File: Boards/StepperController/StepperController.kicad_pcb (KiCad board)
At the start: 2 copper layers, 160 x 100 mm, 131 parts, among them IC1 ATMEGA645A-A, J1 I2C, J2 SPI_Extern, J3 ISP, J4 Reference, J5 Display, J7 Spindle, P1 Power, P10 CONN_Z, P3 USB_B, P4 Relay2, P5 Relay1, P7 EmerOff, P8 CONN_X, P9 CONN_Y, Q1 BC817-40, Q2 BC817-40, Q3 BC817-40, Q4 BC817-40, Q5 BC817-40, SW2 SW_1, SW3 SW_2, U1 LM2595S-5, U3 FT232RL, U4 74LS08, U5 TMC2660, U6 TMC2660, U7 TMC2660, U8 74HC00, X1 16MHz

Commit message: Work in Progress
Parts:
- removed C14: 100nF, Capacitors_SMD:C_0805_HandSoldering
- removed RR1: 10k, w_pth_resistors:r-sil_8
- removed U4: 74LS08, Housings_SOIC:SOIC-14_3.9x8.7mm_Pitch1.27mm
- added D13, D14, D15, D16, D17, D18, D19, D21, D22, D23: 5V, w_smd_diode:sod123, F.Cu at (37.1, 68.1)
- added D20: 6V, w_smd_diode:sod123, F.Cu at (37.1, 68.1)
- added R42: 10k, Resistors_SMD:R_0805_HandSoldering, B.Cu at (197.6, 65.5)
- added R43: 10k, Resistors_SMD:R_0805_HandSoldering, B.Cu at (200.7, 65.5)
- added R44: 10k, Resistors_SMD:R_0805_HandSoldering, B.Cu at (203.7, 65.5)
- added R45: 10k, Resistors_SMD:R_0805_HandSoldering, B.Cu at (206.8, 65.5)
- added R46: 10k, Resistors_SMD:R_0805_HandSoldering, B.Cu at (209.8, 65.5)
- added R47: 10k, Resistors_SMD:R_0805_HandSoldering, B.Cu at (212.9, 65.5)
- added R48: 10k, Resistors_SMD:R_0805_HandSoldering, B.Cu at (215.9, 65.5)
- added R49: 10k, Resistors_SMD:R_0805_HandSoldering, F.Cu at (33.5, 104.1)
- added R50: 10k, Resistors_SMD:R_0805_HandSoldering, F.Cu at (40.1, 104.1)
- added R51: 10k, Resistors_SMD:R_0805_HandSoldering, F.Cu at (33.5, 97.5)
- added R52: 10k, Resistors_SMD:R_0805_HandSoldering, F.Cu at (40.1, 97.5)
- added R53: 100k, Resistors_SMD:R_0805_HandSoldering, F.Cu at (42.2, 110.2)
- added R54: 100k, Resistors_SMD:R_0805_HandSoldering, F.Cu at (26.9, 112.3)
- added R55: 10k, Resistors_SMD:R_0805_HandSoldering, F.Cu at (37.1, 68.1)
- added R56: 4k7, Resistors_SMD:R_0805_HandSoldering, F.Cu at (26.9, 119.4)
- added R57: 4k7, Resistors_SMD:R_0805_HandSoldering, F.Cu at (34.0, 119.4)
- R2, R36, R37, R38, R39, R40, R41: moved to B.Cu
- SW2, SW3: footprint w_switch:smd_push -> SW0773:SW_0773
- X1: footprint Oscillator-Modules:OSCILLATOR_KXO-200_LargePads -> Oscillators:KXO-200_LargePads
- moved R41 231.1 mm to (217.4, 78.2), turned to 90 degrees
- moved R40 228.2 mm to (214.4, 78.2), turned to 90 degrees
- moved R39 225.3 mm to (211.3, 78.2), turned to 90 degrees
- moved R38 222.5 mm to (208.3, 78.2), turned to 90 degrees
- moved R37 219.6 mm to (205.2, 78.2), turned to 90 degrees
- moved R36 216.8 mm to (202.2, 78.2), turned to 90 degrees
- moved R2 214.0 mm to (199.1, 78.2), turned to 90 degrees
- moved C46 71.0 mm to (218.4, 86.9), turned to 270 degrees
- moved U8 70.2 mm to (210.8, 89.4)
- moved C1 27.5 mm to (212.3, 134.1)
- moved J4 12.7 mm to (208.8, 71.1)
- moved SW3 11.6 mm to (174.8, 151.4)
- moved J1 11.2 mm to (186.9, 146.3)
- moved SW2 5.08 mm to (161.5, 151.4)
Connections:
- C2 pad 1: +5V -> Net-(C2-Pad1)
- C7 pad 1: +5V -> Net-(C7-Pad1)
- IC1 pad 34: (no net) -> /Interface/Ref_T1
- IC1 pad 35: /Controller/Ref_X1 -> /Controller/Ref_Z1
- IC1 pad 37: /Controller/Ref_Z1 -> /Controller/Ref_X1
- IC1 pad 41: /Interface/Ref_T1 -> (no net)
- IC1 pad 62: +5V -> Net-(C7-Pad1)
- J5 pad 2: /Controller/SCK -> Net-(J5-Pad2)
- J5 pad 3: /Controller/SDI -> Net-(J5-Pad3)
- J5 pad 4: /Controller/SDO -> Net-(J5-Pad4)
- J5 pad 5: /Interface/CS_Disp -> Net-(J5-Pad5)
- J7 pad 2: /Controller/Spindle_PWM -> Net-(D22-Pad1)
- J7 pad 3: /Interface/Spindle_Enable -> Net-(D23-Pad1)
- L1 pad 2: +5V -> Net-(C2-Pad1)
- P1 pad 1: /Driver/Sup_36V -> (no net)
- R1 pad 1: +5V -> Net-(C2-Pad1)
- U1 pad 4: +5V -> Net-(C2-Pad1)
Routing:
- net /Controller/Ref_X1: track 0.00 -> 142.5 mm, vias 0 -> 3
- net /Controller/Spindle_PWM: track 96.5 -> 0.00 mm, vias 1 -> 0
- net Net-(IC1-Pad40): track 27.5 -> 103.0 mm, vias 0 -> 2
- net /Controller/Stall_Z: track 54.1 -> 127.8 mm, vias 2 -> 4
- net Net-(IC1-Pad39): track 30.4 -> 100.9 mm, vias 0 -> 2
- net /Interface/Spindle_Enable: track 69.4 -> 0.00 mm, vias 1 -> 0
- net Net-(IC1-Pad38): track 35.9 -> 101.9 mm, vias 0 -> 2
- net /Controller/Stall_Y: track 26.3 -> 91.6 mm, vias 2 -> 4
- net +5V: track 257.6 -> 202.7 mm, vias 10 -> 8
- net /Controller/SDI: track 248.4 -> 219.6 mm, vias 7 -> 6
- net Net-(C2-Pad1): track 0.00 -> 17.4 mm
- net /Controller/Ref_Y2: track 0.00 -> 15.6 mm, vias 0 -> 1
- net /Controller/Ref_Z2: track 0.00 -> 14.7 mm, vias 0 -> 1
- net /Controller/Ref_X2: track 0.00 -> 13.2 mm, vias 0 -> 1
- net Net-(D13-Pad1): track 0.01 -> 12.8 mm
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
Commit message: Recover from damaged repository
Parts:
- removed REF**: EuroBoard160mmX100mm_holes, Euro:EuroBoard160mmX100mm_holes
- added D24: D, Diodes_SMD:SOD-123, F.Cu at (90.4, 113.8)
- added D25: D, Diodes_SMD:SOD-123, F.Cu at (86.4, 113.8)
- added F2: 4AT, Fuse_Holders_and_Fuses:Fuseholder5x20_horiz_open_universal_Type-III, F.Cu at (198.6, 160.0)
- C10, C11, C12, C7: moved to F.Cu
- D13, D14, D15, D16, D17, D18, D19, D20: footprint w_smd_diode:sod123 -> Diodes_SMD:SOD-123
- D21, D22, D23: footprint w_smd_diode:sod123 -> Diodes_SMD:SOD-123; moved to B.Cu
- R49, R50, R51, R52: moved to B.Cu
- moved D19 180.1 mm to (216.9, 77.2), turned to 270 degrees
- moved D18 177.5 mm to (214.4, 77.2), turned to 270 degrees
- moved D17 175.0 mm to (211.8, 77.2), turned to 270 degrees
- moved D16 172.5 mm to (209.3, 77.2), turned to 270 degrees
- moved D15 169.9 mm to (206.8, 77.2), turned to 270 degrees
- moved D20 169.2 mm to (193.0, 133.6)
- moved D14 167.4 mm to (204.2, 77.2), turned to 270 degrees
- moved D13 164.8 mm to (201.7, 77.2), turned to 270 degrees
- moved R51 98.6 mm to (122.9, 139.2), turned to 90 degrees
- moved R52 95.0 mm to (125.5, 139.2), turned to 90 degrees
- moved R49 93.7 mm to (120.4, 139.2), turned to 90 degrees
- moved R50 85.3 mm to (117.9, 139.2), turned to 90 degrees
- moved R56 82.9 mm to (105.2, 146.8), turned to 90 degrees
- moved J1 80.9 mm to (106.2, 140.7)
- moved R57 78.6 mm to (107.7, 146.8), turned to 90 degrees
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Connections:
- D1 pad 2: (no net) -> GND
- IC1 pad 10: (no net) -> /Interface/CS_Disp
- IC1 pad 14: Net-(IC1-Pad14) -> (no net)
- IC1 pad 15: Net-(IC1-Pad15) -> (no net)
- IC1 pad 16: Net-(IC1-Pad16) -> (no net)
- IC1 pad 26: /Controller/Emergency_Off -> (no net)
- IC1 pad 27: /Interface/Spindle_Enable -> Net-(IC1-Pad27)
- IC1 pad 28: /Controller/Enable -> Net-(IC1-Pad28)
- IC1 pad 29: (no net) -> Net-(IC1-Pad29)
- IC1 pad 43: /Interface/CS_Disp -> (no net)
- IC1 pad 54: (no net) -> /Interface/Spindle_Enable
- IC1 pad 55: (no net) -> /Controller/Enable
- IC1 pad 56: (no net) -> /Controller/Emergency_Off
- J2 pad 5: Net-(IC1-Pad14) -> Net-(IC1-Pad27)
- J2 pad 6: Net-(IC1-Pad15) -> Net-(IC1-Pad28)
- J2 pad 7: Net-(IC1-Pad16) -> Net-(IC1-Pad29)
- P1 pad 1: (no net) -> /Driver/Sup_36V
- R1 pad 1: Net-(C2-Pad1) -> +5V
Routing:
- net /Interface/Ref_T1: track 1.06 -> 119.4 mm, vias 0 -> 3
- net /Controller/Ref_Y1: track 2.65 -> 119.0 mm, vias 0 -> 3
- net /Controller/Ref_Z1: track 1.52 -> 116.6 mm, vias 0 -> 3
- net /Controller/Spindle_PWM: track 0.00 -> 64.4 mm, vias 0 -> 2
- net Net-(IC1-Pad9): track 0.00 -> 62.7 mm
- net Net-(IC1-Pad29): track 0.00 -> 52.6 mm, vias 0 -> 1
- net Net-(IC1-Pad28): track 0.00 -> 50.3 mm, vias 0 -> 1
- net Net-(IC1-Pad27): track 0.00 -> 48.9 mm, vias 0 -> 1
- net Net-(IC1-Pad8): track 0.00 -> 48.7 mm
- net /Controller/SCK: track 209.0 -> 255.1 mm, vias 6 -> 8
- net /Interface/Spindle_Enable: track 0.00 -> 45.6 mm
- net +5V: track 202.7 -> 245.0 mm, vias 8 -> 6
- net /Controller/SDI: track 219.6 -> 259.8 mm
- net /Controller/SDO: track 202.2 -> 240.2 mm, vias 4 -> 6
- net Net-(D4-Pad2): track 0.00 -> 29.9 mm, vias 0 -> 1
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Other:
- board outline removed

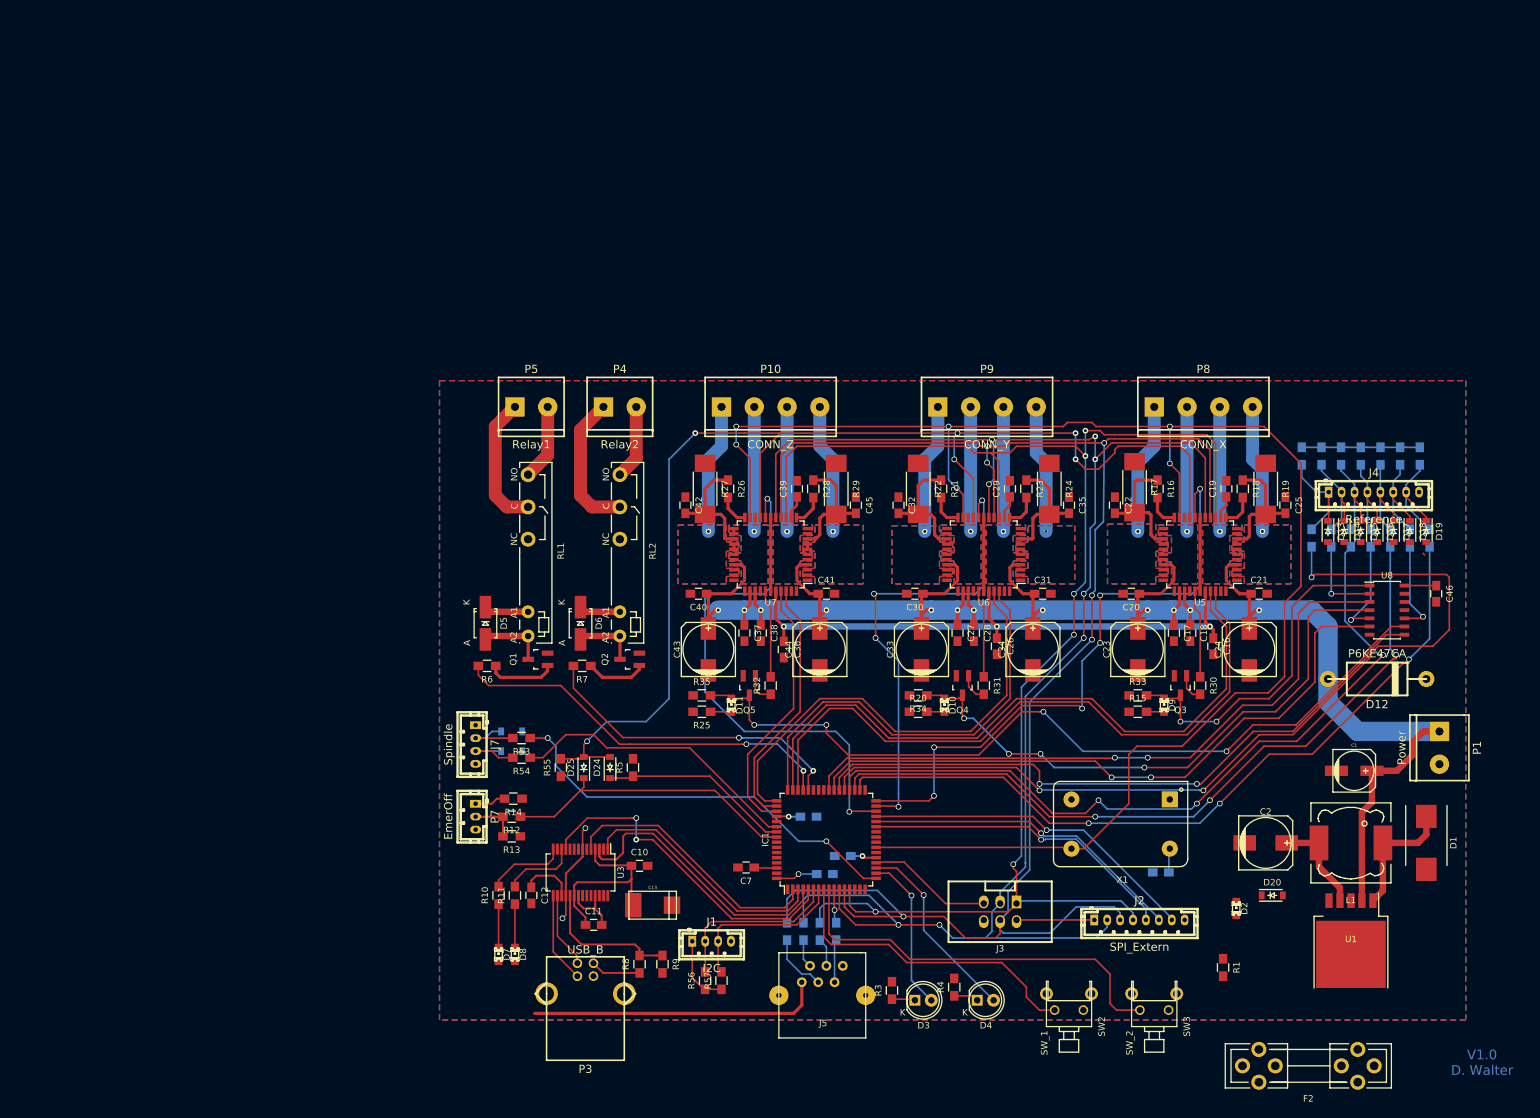
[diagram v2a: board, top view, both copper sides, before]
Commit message: Cover-Anschluss hinzu, Schutzdioden geändert
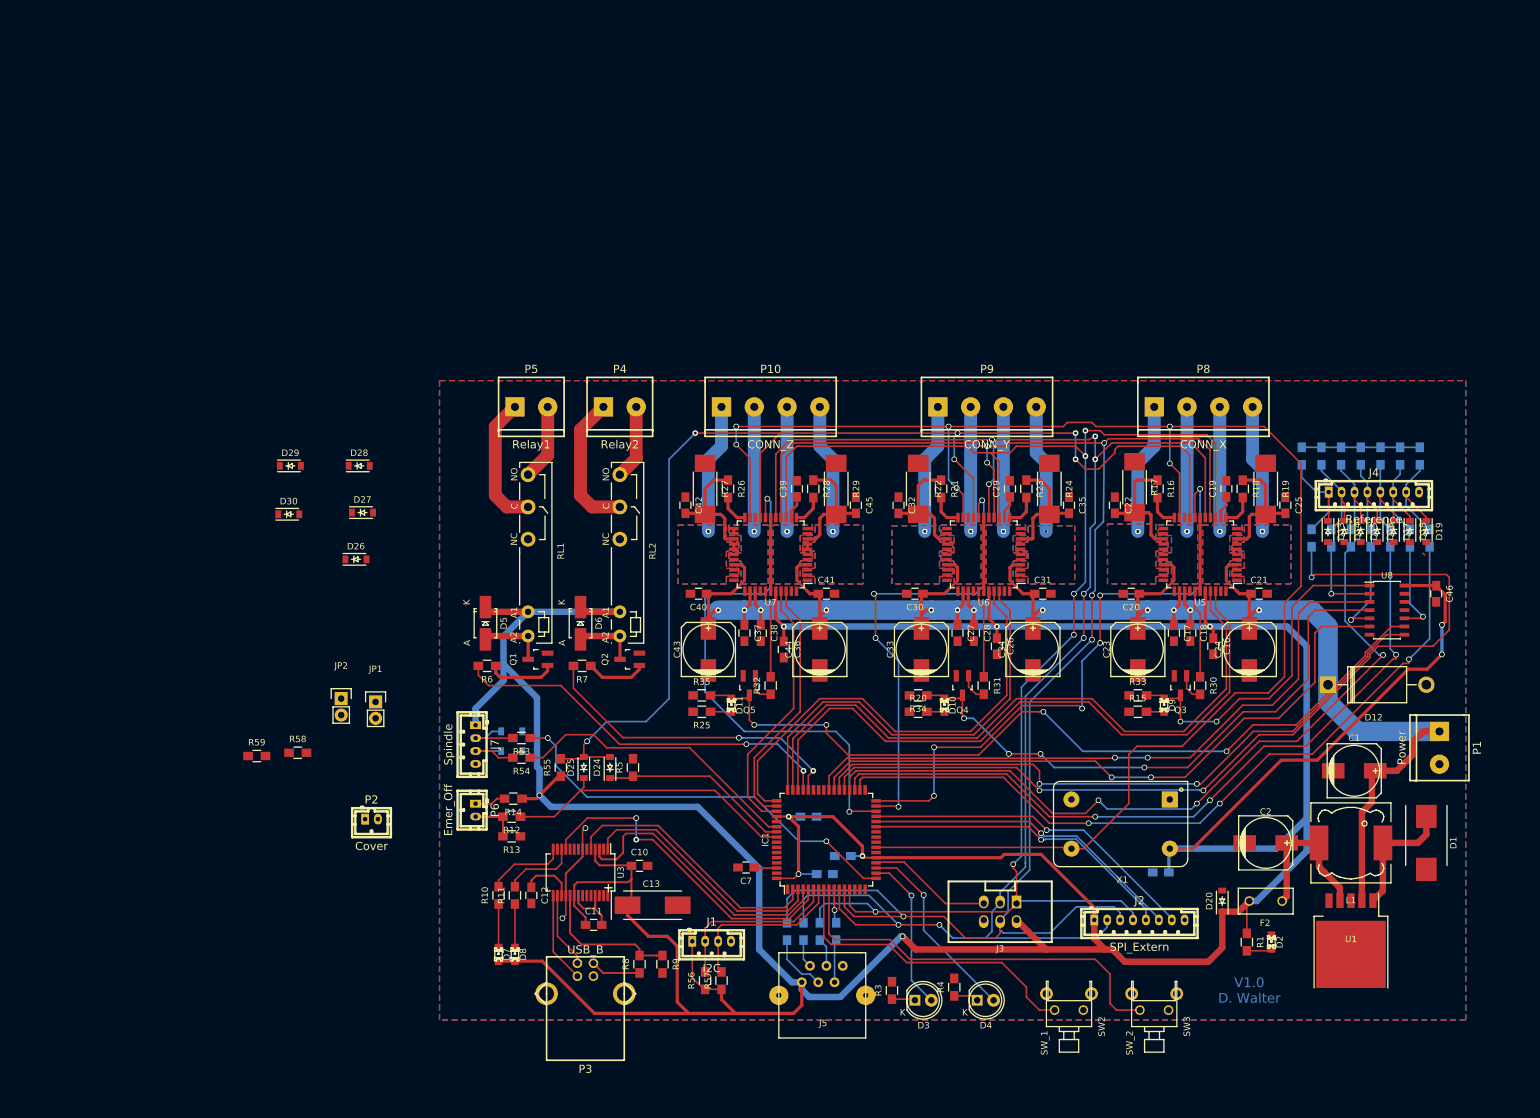
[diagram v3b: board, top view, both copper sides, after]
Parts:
- removed P7: EmerOff, w_conn_jst-ph:b3b-ph-kl
- added D26: D, Diodes_SMD:SOD-123, F.Cu at (51.1, 81.5)
- added D27: D, Diodes_SMD:SOD-123, F.Cu at (52.1, 74.3)
- added D28: D, Diodes_SMD:SOD-123, F.Cu at (51.6, 67.1)
- added D29: 5V, Diodes_SMD:SOD-123, F.Cu at (40.9, 67.1)
- added D30: D, Diodes_SMD:SOD-123, F.Cu at (40.6, 74.5)
- added JP1: JUMPER, Pin_Headers:Pin_Header_Straight_1x02, F.Cu at (54.1, 103.6)
- added JP2: JUMPER, Pin_Headers:Pin_Header_Straight_1x02, F.Cu at (48.8, 103.1)
- added P2: Cover, w_conn_jst-ph:b2b-ph-kl, F.Cu at (53.5, 121.8)
- added P6: Emer_Off, w_conn_jst-ph:b2b-ph-kl, F.Cu at (69.6, 120.4)
- added R58: 100R, Resistors_SMD:R_0805_HandSoldering, F.Cu at (42.0, 111.5)
- added R59: 100R, Resistors_SMD:R_0805_HandSoldering, F.Cu at (35.7, 112.0)
- C1: footprint w_smd_cap:c_elec_6.3x7.7 -> Capacitors_SMD:c_elec_8x10.5
- C13: footprint w_smd_cap:c_tant_D -> Capacitors_Tantalum_SMD:TantalC_SizeD_EIA-7343_HandSoldering
- D12: footprint w_pth_diodes:diode_do201 -> Diodes_ThroughHole:Diode_DO-201AD_Horizontal_RM15
- F2: footprint Fuse_Holders_and_Fuses:Fuseholder5x20_horiz_open_universal_Type-III -> Fuse_Holders_and_Fuses:Fuse_TE5_Littlefuse-395Series
- R12, R2, R36, R37, R38, R39, R40, R41, R53, R54: value 100k -> 100R
- R13: value 5k -> 1k
- R42, R43, R44, R45, R46, R47, R48, R49, R5, R51: value 10k -> 1k
- R52: value 10k -> 100R
- moved F2 26.4 mm to (192.0, 134.5)
- moved D20 7.80 mm to (185.3, 134.5), turned to 90 degrees
- moved D12 7.67 mm to (201.7, 101.0)
- moved D2 7.55 mm to (192.9, 140.8)
- moved R1 5.39 mm to (189.1, 140.8)
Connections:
- D13 pad 1: Net-(D13-Pad1) -> /Controller/Ref_X1
- D14 pad 1: Net-(D14-Pad1) -> /Controller/Ref_X2
- D15 pad 1: Net-(D15-Pad1) -> /Controller/Ref_Y1
- D16 pad 1: Net-(D16-Pad1) -> /Controller/Ref_Y2
- D17 pad 1: Net-(D17-Pad1) -> /Controller/Ref_Z1
- D18 pad 1: Net-(D18-Pad1) -> /Controller/Ref_Z2
- D19 pad 1: Net-(D19-Pad1) -> /Interface/Ref_T1
- D21 pad 1: Net-(D21-Pad1) -> /Controller/Emergency_Off
- D22 pad 1: Net-(D22-Pad1) -> /Controller/Spindle_PWM
- IC1 pad 57: (no net) -> /Controller/Cover
- J4 pad 1: Net-(D13-Pad1) -> Net-(J4-Pad1)
- J4 pad 2: Net-(D14-Pad1) -> Net-(J4-Pad2)
- J4 pad 3: Net-(D15-Pad1) -> Net-(J4-Pad3)
- J4 pad 4: Net-(D16-Pad1) -> Net-(J4-Pad4)
- J4 pad 5: Net-(D17-Pad1) -> Net-(J4-Pad5)
- J4 pad 6: Net-(D18-Pad1) -> Net-(J4-Pad6)
- J4 pad 7: Net-(D19-Pad1) -> Net-(J4-Pad7)
- J5 pad 2: Net-(J5-Pad2) -> /Controller/SCK
- J5 pad 3: Net-(J5-Pad3) -> /Controller/SDI
- J5 pad 4: Net-(J5-Pad4) -> /Controller/SDO
- J5 pad 5: Net-(J5-Pad5) -> /Interface/CS_Disp
- J7 pad 1: +5V -> Net-(J7-Pad1)
- J7 pad 2: Net-(D22-Pad1) -> Net-(J7-Pad2)
- J7 pad 3: Net-(D23-Pad1) -> Net-(J7-Pad3)
- R12 pad 2: Net-(D21-Pad1) -> Net-(P6-Pad2)
- R13 pad 2: Net-(D21-Pad1) -> /Controller/Emergency_Off
- R2 pad 2: Net-(D13-Pad1) -> Net-(J4-Pad1)
- R36 pad 2: Net-(D14-Pad1) -> Net-(J4-Pad2)
- R37 pad 2: Net-(D15-Pad1) -> Net-(J4-Pad3)
- R38 pad 2: Net-(D16-Pad1) -> Net-(J4-Pad4)
- R39 pad 2: Net-(D17-Pad1) -> Net-(J4-Pad5)
- R40 pad 2: Net-(D18-Pad1) -> Net-(J4-Pad6)
- R41 pad 2: Net-(D19-Pad1) -> Net-(J4-Pad7)
- R42 pad 2: Net-(D13-Pad1) -> Net-(J4-Pad1)
- R43 pad 2: Net-(D14-Pad1) -> Net-(J4-Pad2)
- R44 pad 2: Net-(D15-Pad1) -> Net-(J4-Pad3)
- R45 pad 2: Net-(D16-Pad1) -> Net-(J4-Pad4)
- R46 pad 2: Net-(D17-Pad1) -> Net-(J4-Pad5)
- R47 pad 2: Net-(D18-Pad1) -> Net-(J4-Pad6)
- R48 pad 2: Net-(D19-Pad1) -> Net-(J4-Pad7)
- R49 pad 1: Net-(J5-Pad2) -> /Interface/Spindle_Enable
- R49 pad 2: /Controller/SCK -> GND
- R50 pad 1: Net-(J5-Pad3) -> +5V
- R50 pad 2: /Controller/SDI -> Net-(D23-Pad1)
- R51 pad 1: Net-(J5-Pad4) -> GND
- R51 pad 2: /Controller/SDO -> /Controller/Cover
- R52 pad 1: Net-(J5-Pad5) -> /Controller/Cover
- R52 pad 2: /Interface/CS_Disp -> Net-(P2-Pad2)
- R53 pad 2: Net-(D22-Pad1) -> Net-(J7-Pad2)
- R54 pad 1: /Interface/Spindle_Enable -> Net-(D23-Pad1)
- R54 pad 2: Net-(D23-Pad1) -> Net-(J7-Pad3)
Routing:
- net +5V: track 245.0 -> 626.2 mm, vias 6 -> 9
- net Net-(J7-Pad1): track 0.00 -> 89.8 mm, vias 0 -> 1
- net /Controller/SDI: track 259.8 -> 237.6 mm
- net GND: track 59.1 -> 81.0 mm
- net /Controller/SCK: track 255.1 -> 236.0 mm
- net Net-(D13-Pad1): track 18.4 -> 0.00 mm
- net Net-(D19-Pad1): track 18.1 -> 0.00 mm
- net Net-(J4-Pad7): track 0.00 -> 17.6 mm
- net Net-(D18-Pad1): track 17.0 -> 0.00 mm
- net Net-(D14-Pad1): track 16.8 -> 0.00 mm
- net Net-(J4-Pad6): track 0.00 -> 16.3 mm
- net Net-(D17-Pad1): track 16.0 -> 0.00 mm
- net Net-(D15-Pad1): track 16.0 -> 0.00 mm
- net Net-(D23-Pad1): track 10.1 -> 25.9 mm
- net Net-(D16-Pad1): track 15.7 -> 0.00 mm
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
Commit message: Layouting...
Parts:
- removed D24, D25, D26, D27, D28, D30: D, Diodes_SMD:SOD-123
- removed R50, R55: 10k, Resistors_SMD:R_0805_HandSoldering
- added C14: 100nF, Capacitors_SMD:C_0805_HandSoldering, B.Cu at (175.8, 121.9)
- added C3: 100nF, Capacitors_SMD:C_0805_HandSoldering, F.Cu at (87.4, 117.3)
- added C9: 12pF, Capacitors_SMD:C_0805_HandSoldering, F.Cu at (146.1, 121.9)
- added U2: 74LS11, Housings_SOIC:SOIC-14_3.9x8.7mm_Pitch1.27mm, F.Cu at (96.5, 113.8)
- added Y1: 20MHz, w_crystal:hc-49_smd, F.Cu at (142.7, 126.0)
- C13, D29, R14, R56, R57, R58, R8, R9: moved to B.Cu
- C8: value 100nF -> 12pF; moved to F.Cu
- JP1, JP2: value JUMPER -> JUMPER3; footprint Pin_Headers:Pin_Header_Straight_1x02 -> Socket_Strips:Socket_Strip_Straight_1x03
- R42, R43, R44, R45, R46, R47, R48, R49, R51, R52: moved to F.Cu
- X1: footprint Oscillators:KXO-200_LargePads -> Oscillators:OSC_DIP8
- moved D29 66.7 mm to (85.3, 116.8)
- moved R52 53.9 mm to (75.7, 118.5), turned to 180 degrees
- moved R51 53.2 mm to (75.7, 114.7), turned to 0 degrees
- moved R59 40.2 mm to (74.9, 103.5), turned to 180 degrees
- moved JP2 35.1 mm to (83.8, 105.2)
- moved C8 33.5 mm to (142.2, 130.0), turned to 0 degrees
- moved R58 33.5 mm to (75.2, 116.3), turned to 180 degrees
- moved JP1 31.1 mm to (83.8, 112.8)
- moved R49 23.8 mm to (109.0, 118.4), turned to 270 degrees
- moved D21 23.7 mm to (98.7, 124.6), turned to 270 degrees
- moved R9 16.5 mm to (82.8, 139.4)
- moved P2 16.3 mm to (69.2, 117.5), turned to 270 degrees
- moved R6 14.5 mm to (85.9, 98.0), turned to 0 degrees
- moved J2 13.6 mm to (166.2, 125.3), turned to 90 degrees
- moved D20 12.9 mm to (186.4, 147.3), turned to 270 degrees
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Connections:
- C8 pad 1: +5V -> Net-(C8-Pad1)
- IC1 pad 23: /Controller/TMC_Clock -> Net-(C8-Pad1)
- IC1 pad 24: (no net) -> Net-(C9-Pad1)
- IC1 pad 54: /Interface/Spindle_Enable -> /Controller/Enable
- IC1 pad 55: /Controller/Enable -> /Interface/Spindle_Enable
- R49 pad 1: /Interface/Spindle_Enable -> /Controller/Enable
- R5 pad 1: /Controller/Enable -> /Interface/Spindle_Enable
- U5 pad 21: /Controller/TMC_Clock -> /Driver/Driver_X/TMC_Clock
- U6 pad 21: /Controller/TMC_Clock -> /Driver/Driver_X/TMC_Clock
- U7 pad 21: /Controller/TMC_Clock -> /Driver/Driver_X/TMC_Clock
- X1 pad 8: /Controller/TMC_Clock -> +5V
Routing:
- net /Controller/TMC_Clock: track 248.1 -> 0.00 mm, vias 6 -> 0
- net /Driver/Driver_X/TMC_Clock: track 0.00 -> 193.6 mm, vias 0 -> 7
- net Net-(J7-Pad1): track 89.8 -> 4.37 mm, vias 1 -> 0
- net /Controller/Cover: track 3.64 -> 64.3 mm
- net GND: track 81.0 -> 43.6 mm, vias 2 -> 0
- net Net-(JP2-Pad2): track 0.00 -> 24.4 mm
- net /Interface/Spindle_Enable: track 46.6 -> 22.8 mm
- net Net-(C9-Pad1): track 0.00 -> 17.1 mm
- net /Controller/CTS: track 51.7 -> 35.6 mm
- net /Controller/RXD: track 41.3 -> 26.7 mm
- net Net-(JP1-Pad2): track 0.00 -> 14.3 mm
- net Net-(J4-Pad4): track 14.0 -> 28.2 mm
- net Net-(IC1-Pad29): track 52.6 -> 38.6 mm, vias 1 -> 0
- net Net-(J4-Pad6): track 16.3 -> 30.1 mm
- net Net-(J4-Pad3): track 13.7 -> 27.4 mm
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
